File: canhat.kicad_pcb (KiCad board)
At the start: 2 copper layers, 65 x 30 mm, 37 parts, among them J1 Raspberry_Pi_2_3, J2 CAN In/Out/GND, J5 12V, U1 MCP2515-xSO, U2 SN65HVD234, U3 AT24C32-SSHM, U4 AP63205, Y1 16MHz

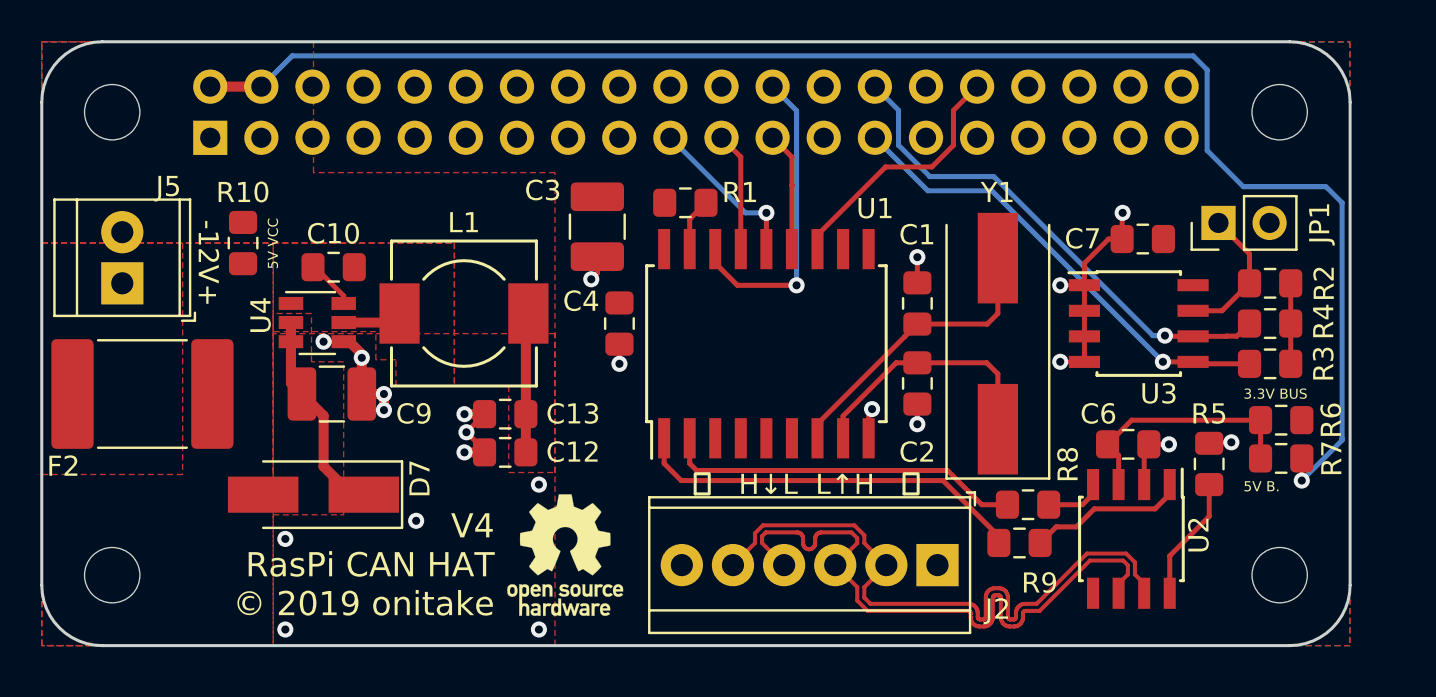
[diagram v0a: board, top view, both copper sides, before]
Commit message: Added GPIO pullups
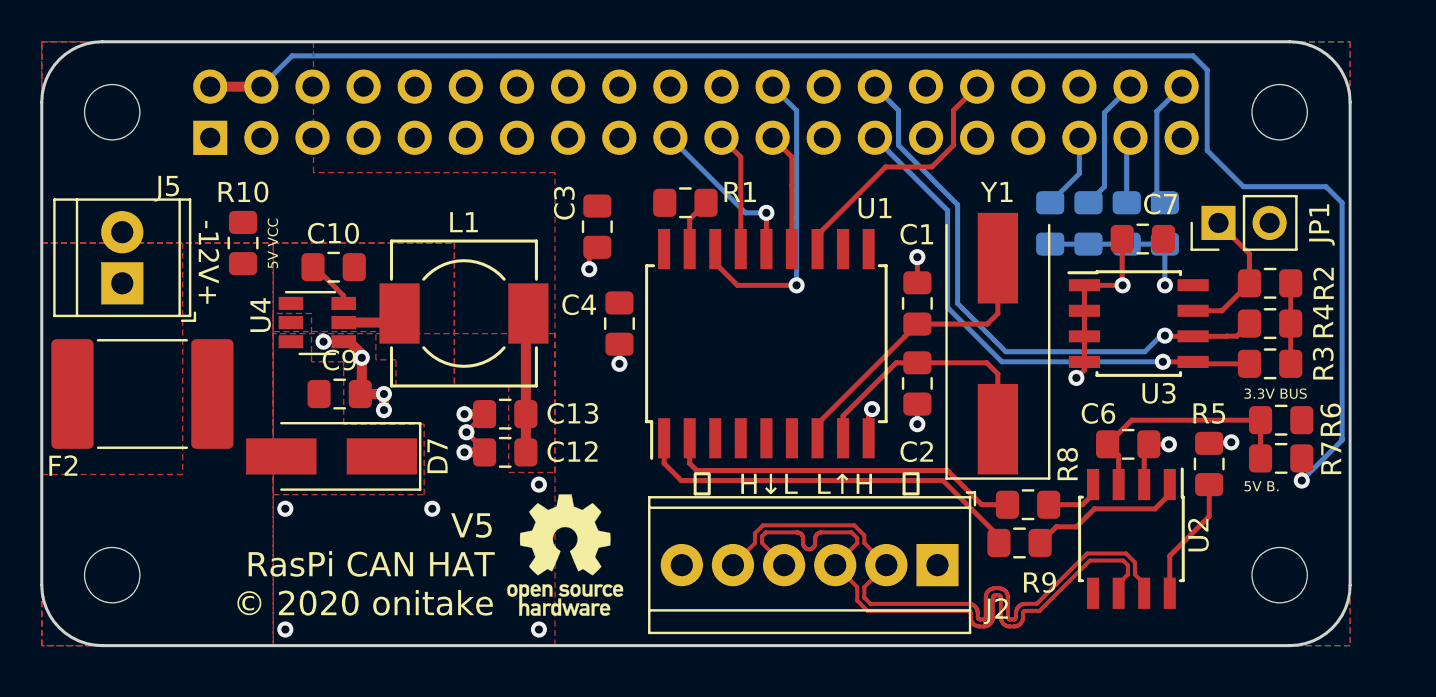
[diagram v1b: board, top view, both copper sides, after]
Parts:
- added R11: 1k, Resistor_SMD:R_0805_2012Metric_Pad1.15x1.40mm_HandSolder, B.Cu at (95.8, 59.0)
- added R12: 1k, Resistor_SMD:R_0805_2012Metric_Pad1.15x1.40mm_HandSolder, B.Cu at (92.0, 59.0)
- added R13: 1k, Resistor_SMD:R_0805_2012Metric_Pad1.15x1.40mm_HandSolder, B.Cu at (93.9, 59.0)
- added R14: 1k, Resistor_SMD:R_0805_2012Metric_Pad1.15x1.40mm_HandSolder, B.Cu at (90.1, 59.0)
- C3, C9: footprint Capacitor_SMD:C_1210_3225Metric_Pad1.42x2.65mm_HandSolder -> Capacitor_SMD:C_0805_2012Metric_Pad1.15x1.40mm_HandSolder
- moved D7 2.10 mm to (54.4, 70.6)
- moved C9 0.39 mm to (54.8, 67.5)
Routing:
- net Net-(C9-Pad1): track 13.2 -> 0.00 mm
- net +3V3: track 4.04 -> 11.8 mm, vias 0 -> 1
- net /GPIO20: track 0.00 -> 6.64 mm
- net /GPIO21: track 0.00 -> 6.45 mm
- net /GPIO19: track 0.00 -> 3.83 mm
- net /ID_SC: track 25.2 -> 28.8 mm
- net /GPIO26: track 0.00 -> 3.31 mm
- net /ID_SD: track 23.3 -> 26.1 mm
- net GND: track 31.9 -> 29.9 mm, vias 22 -> 21
- net +12V: track 0.00 -> 1.50 mm
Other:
- board text added: "V5 RasPi CAN HAT © 2020 onitake"
- board text removed: "V4 RasPi CAN HAT © 2019 onitake"

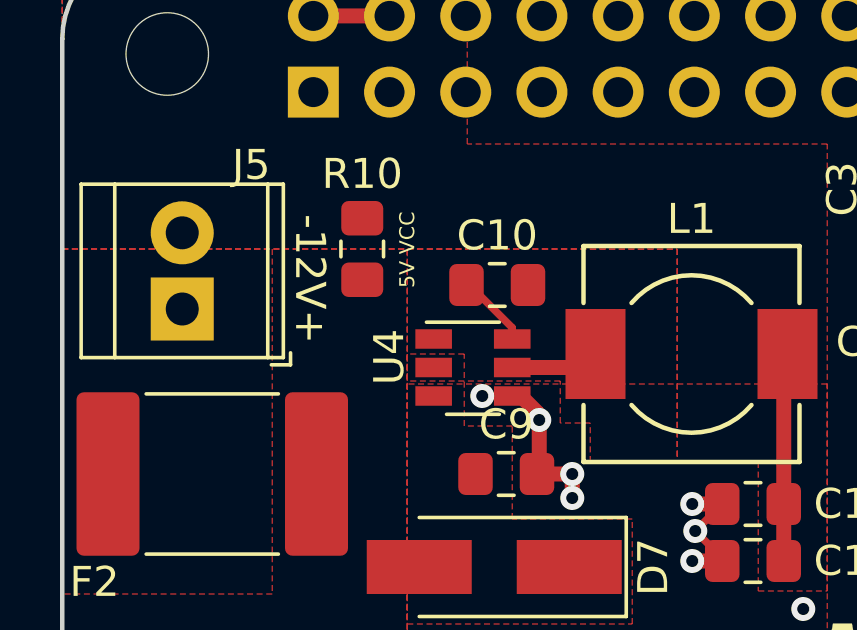
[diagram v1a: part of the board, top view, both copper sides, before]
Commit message: Fixed incorrect feedback pin wire
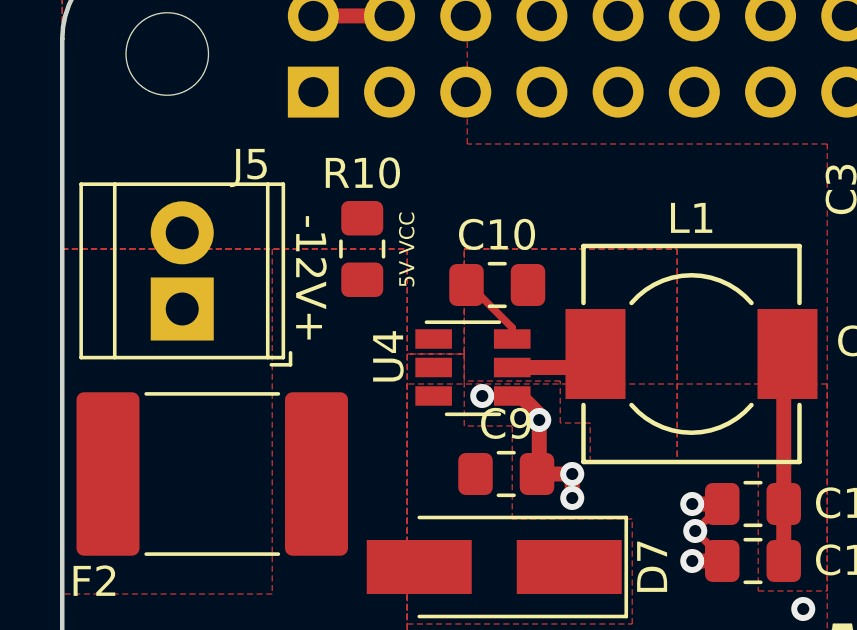
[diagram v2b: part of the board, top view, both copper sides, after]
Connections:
- R12 pad 1: /GPIO20 -> /GPIO26
- R13 pad 1: /GPIO26 -> /GPIO20
- U4 pad 1: Net-(C10-Pad2) -> +5V

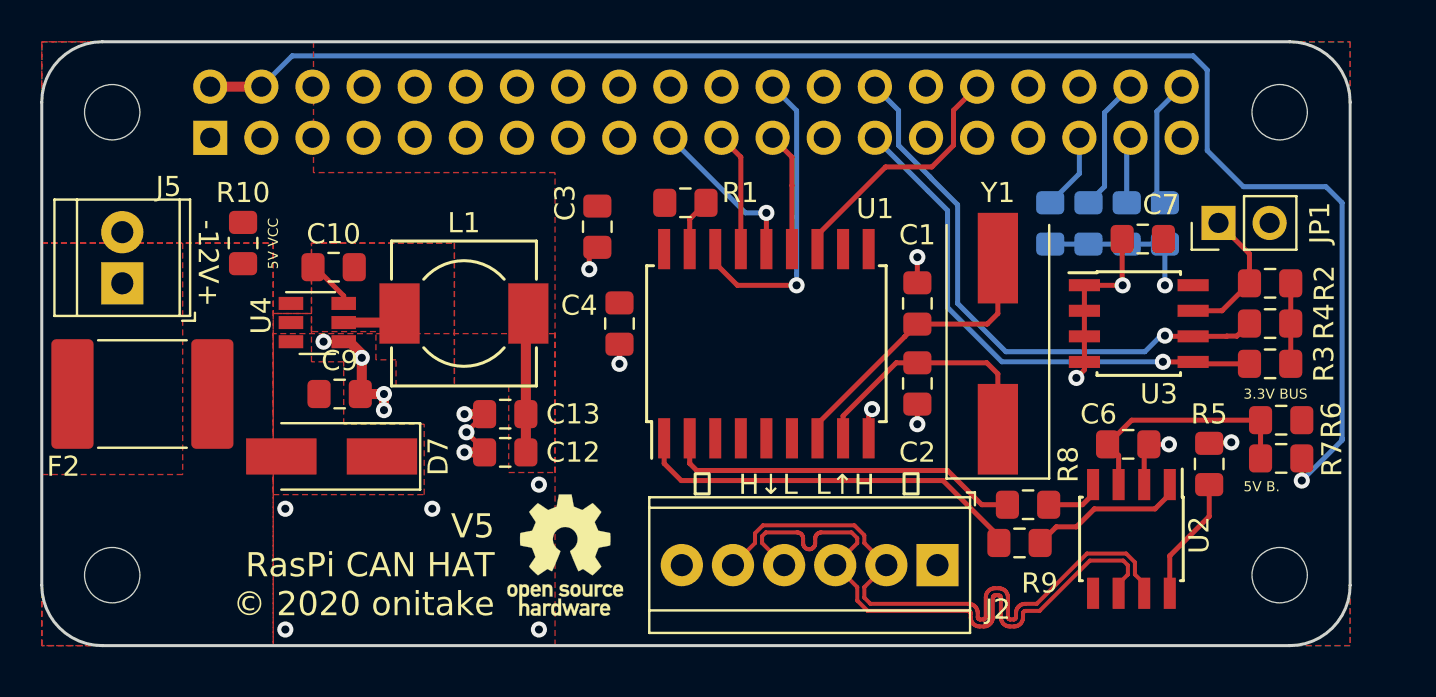
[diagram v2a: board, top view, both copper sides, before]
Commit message: Reordered parts an added GPIO pins
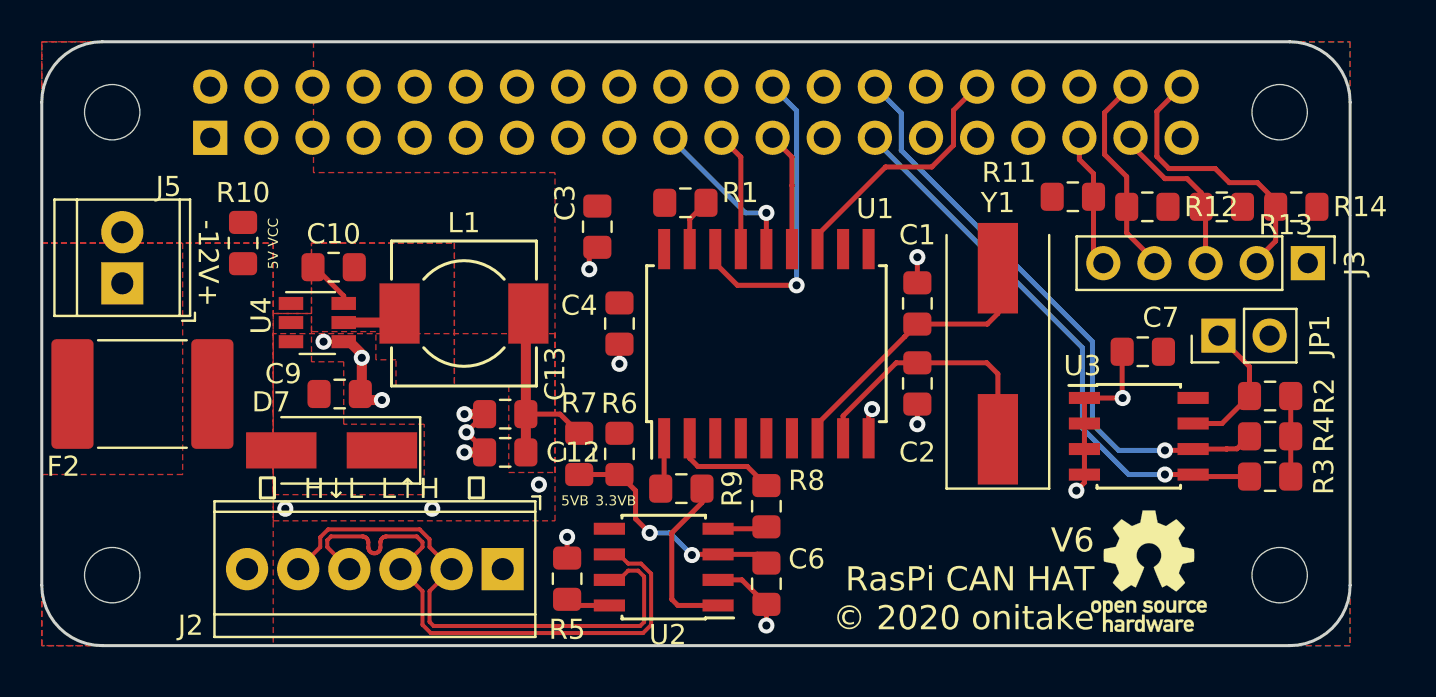
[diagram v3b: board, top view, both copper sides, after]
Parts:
- added J3: GPIO, Connector_PinHeader_2.54mm:PinHeader_1x05_P2.54mm_Vertical, F.Cu at (102.9, 61.0)
- R11, R12, R13, R14: moved to F.Cu
- moved R7 34.9 mm to (66.7, 70.5), turned to 270 degrees
- moved R6 32.9 mm to (68.7, 70.5), turned to 90 degrees
- moved R5 32.4 mm to (66.1, 76.7)
- moved OSHW1 29.0 mm to (95.0, 76.3)
- moved U2 23.3 mm to (70.9, 76.1), turned to 180 degrees
- moved J2 21.6 mm to (62.9, 76.2)
- moved C6 19.3 mm to (76.0, 76.9), turned to 270 degrees
- moved R9 17.0 mm to (71.8, 72.2)
- moved R8 13.0 mm to (76.0, 73.1), turned to 270 degrees
- moved R14 12.3 mm to (102.3, 58.2), turned to 0 degrees
- moved C7 5.60 mm to (94.7, 65.4)
- moved JP1 5.60 mm to (98.5, 64.6)
- moved R2 5.60 mm to (101.0, 67.6)
- moved R3 5.60 mm to (101.0, 71.6)
- moved R4 5.60 mm to (101.0, 69.6)
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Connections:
- D7 pad 2: +12V -> +12LF
- F2 pad 1: Net-(F2-Pad1) -> +12V
- F2 pad 2: +12V -> +12LF
- J5 pad 1: Net-(F2-Pad1) -> +12V
- R10 pad 2: +12V -> +12LF
- R11 pad 1: /GPIO21 -> /GPIO19
- R12 pad 1: /GPIO26 -> /GPIO20
- R13 pad 1: /GPIO20 -> /GPIO26
- R14 pad 1: /GPIO19 -> /GPIO21
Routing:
- net +5V: track 84.8 -> 9.89 mm, vias 1 -> 0
- net Net-(R9-Pad1): track 20.0 -> 2.57 mm
- net Net-(R8-Pad1): track 17.9 -> 5.36 mm
- net /GPIO21: track 6.45 -> 14.3 mm
- net +3V3: track 11.8 -> 4.04 mm, vias 1 -> 0
- net /GPIO26: track 3.31 -> 8.69 mm
- net /CAN_P: track 32.0 -> 28.0 mm
- net Net-(R5-Pad2): track 6.21 -> 2.23 mm
- net /GPIO20: track 6.64 -> 10.3 mm
- net /GPIO19: track 3.83 -> 6.72 mm
- net /CAN_N: track 32.0 -> 29.7 mm
- net /ID_SD: track 26.1 -> 28.0 mm
- net +12V: track 1.50 -> 0.00 mm
- net +12LF: track 0.00 -> 1.50 mm
- net /ID_SC: track 28.8 -> 30.1 mm
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- added copper zone on F.Cu, net +12LF
- removed copper zone on F.Cu, net Net-(F2-Pad1)
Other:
- board text added: "3.3VB"
- board text added: "5VB"
- board text added: "V6 RasPi CAN HAT © 2020 onitake"
- board text removed: "3.3V BUS"
- board text removed: "5V B."
- board text removed: "V5 RasPi CAN HAT © 2020 onitake"

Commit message: Move parts a bit
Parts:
- moved R11 0.92 mm to (90.3, 57.7)
- moved C12 0.80 mm to (63.0, 69.6)
- moved C10 0.80 mm to (54.5, 60.4)
- moved U4 0.80 mm to (53.7, 63.1)
- moved C13 0.80 mm to (63.0, 67.7)
- moved C9 0.80 mm to (54.8, 66.7)
- moved D7 0.80 mm to (54.4, 69.5)
- moved L1 0.80 mm to (61.0, 62.7)
- moved R14 0.73 mm to (101.6, 58.2)
- moved R12 0.72 mm to (94.2, 58.2)
- moved R13 0.72 mm to (97.9, 58.2)
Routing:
- net GND: track 30.0 -> 20.2 mm, vias 18 -> 14
- net +12LF: track 1.50 -> 5.01 mm
- net /GPIO21: track 14.3 -> 13.3 mm
- net /CAN_N: track 29.7 -> 28.8 mm
- net /CAN_P: track 28.0 -> 28.8 mm
- net /GPIO26: track 8.69 -> 8.04 mm
- net /TX: track 8.55 -> 8.05 mm, vias 0 -> 2
- net VBUS: track 12.0 -> 12.1 mm, vias 2 -> 0
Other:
- board text added: "CAN HAT V6 Raspberry Pi ©2020 onitake"
- board text removed: "V6 RasPi CAN HAT © 2020 onitake"

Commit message: More finetuning
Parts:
- moved OSHW1 13.9 mm to (81.1, 76.0)
- moved R5 1.47 mm to (66.1, 75.2)
- moved Y1 0.70 mm to (87.5, 66.2)
- moved R11 0.54 mm to (90.1, 58.2)
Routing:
- net GND: track 20.2 -> 17.9 mm, vias 14 -> 18
- net Net-(C1-Pad1): track 14.7 -> 12.6 mm
- net /ID_SD: track 28.0 -> 29.1 mm
- net Net-(R5-Pad2): track 2.23 -> 3.23 mm
- net +5V: track 9.50 -> 8.55 mm
- net /TX: track 8.05 -> 7.22 mm, vias 2 -> 0
- net VBUS: track 12.1 -> 12.8 mm, vias 0 -> 2
- net Net-(C2-Pad2): track 12.9 -> 13.6 mm
- net /ID_SC: track 30.1 -> 30.6 mm

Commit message: Some more finetunings
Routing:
- net GND: vias 18 -> 17

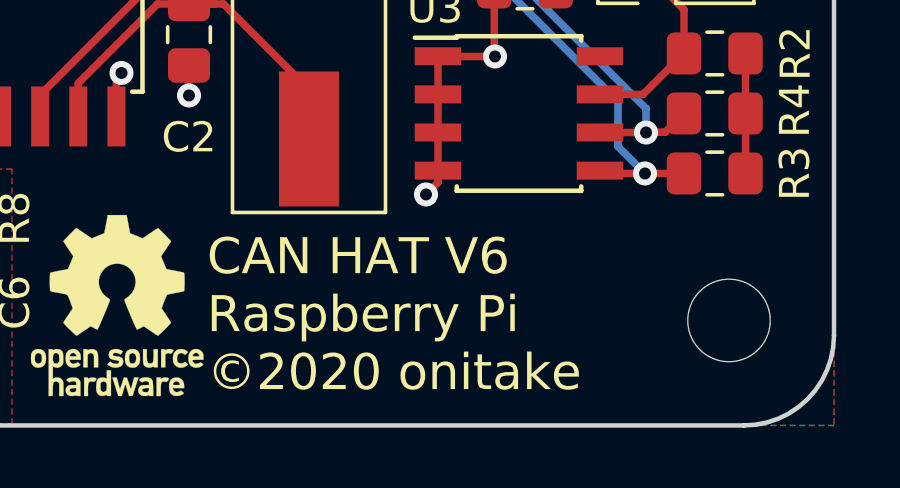
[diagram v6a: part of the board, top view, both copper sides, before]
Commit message: Corrected Raspberry Pi branding
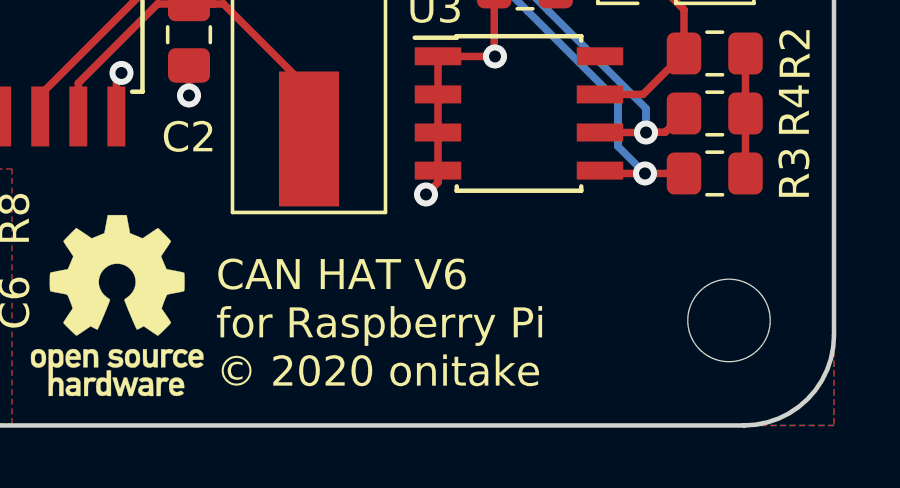
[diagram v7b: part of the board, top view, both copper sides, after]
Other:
- board text added: "CAN HAT V6 for Raspberry Pi © 2020 onitake"
- board text removed: "CAN HAT V6 Raspberry Pi ©2020 onitake"

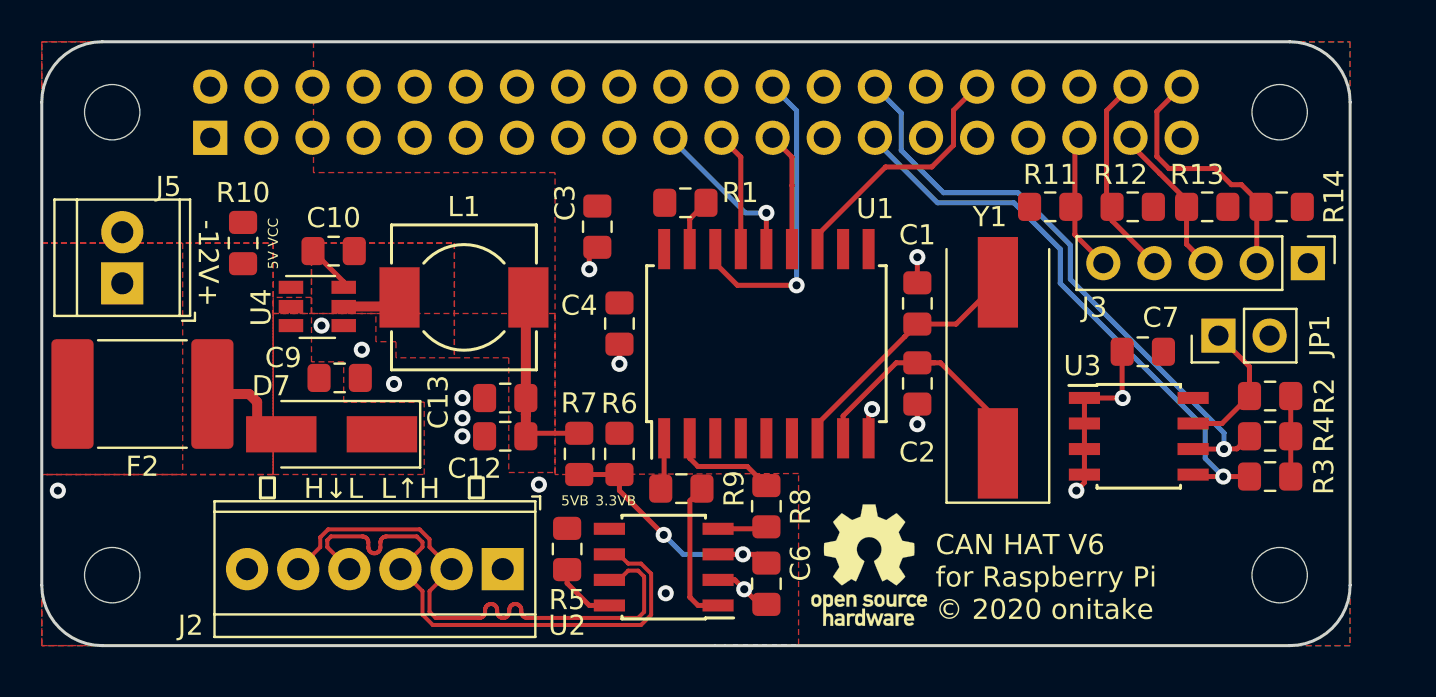
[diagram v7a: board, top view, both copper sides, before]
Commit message: Use 5V transceiver with 3V logic and some finetuning
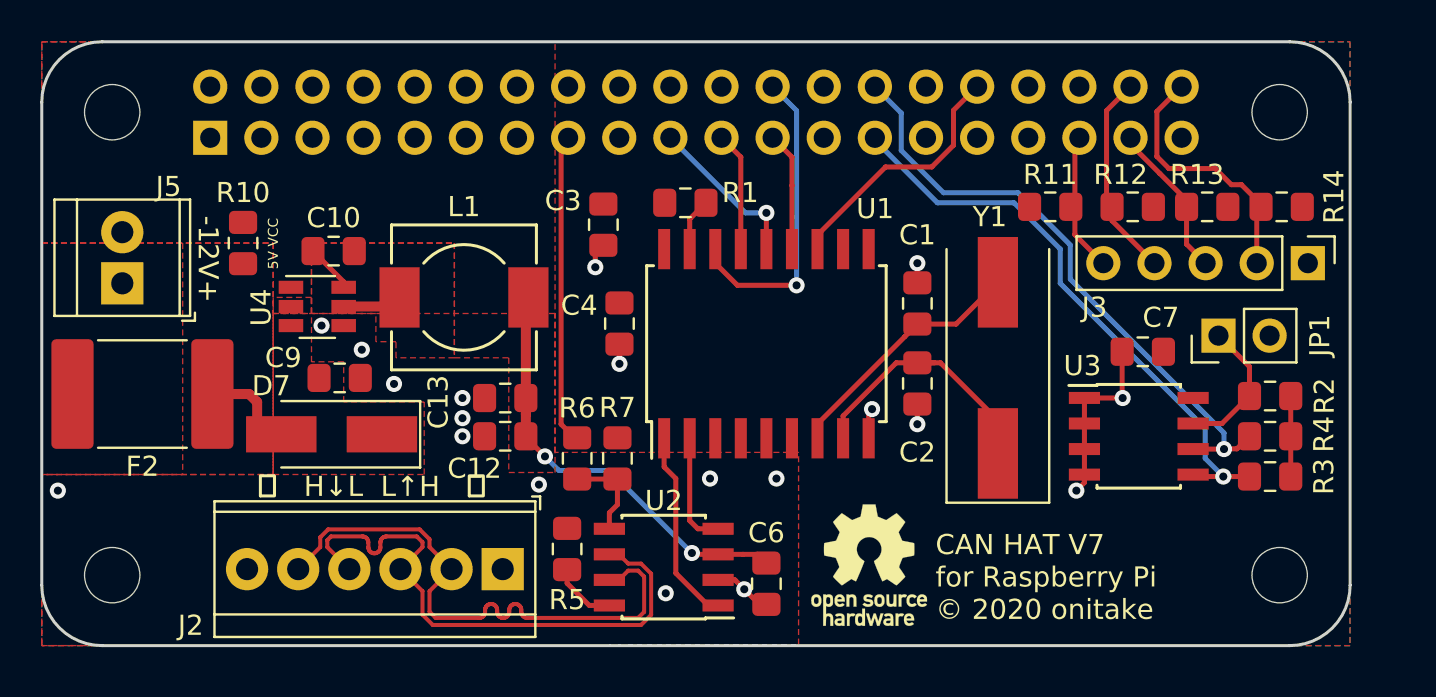
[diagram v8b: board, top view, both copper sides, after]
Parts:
- removed R8, R9: 1k, Resistor_SMD:R_0805_2012Metric_Pad1.15x1.40mm_HandSolder
- R6: value DNP/0 -> DNP
- R7: value 0/DNP -> 0
- U2: value SN65HVD234 -> SN65HVDA541
- moved R6 2.11 mm to (66.6, 70.7)
- moved R7 1.91 mm to (68.6, 70.7)
- moved C3 0.32 mm to (67.9, 59.1)
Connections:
- C6 pad 1: VBUS -> +5V
- J1 pad 15: (no net) -> /TRXEN
- R6 pad 1: VBUS -> Net-(R6-Pad1)
- R6 pad 2: +3V3 -> /TRXEN
- R7 pad 1: +5V -> +3V3
- R7 pad 2: VBUS -> Net-(R6-Pad1)
- U1 pad 1: Net-(R9-Pad1) -> /TX
- U1 pad 2: Net-(R8-Pad1) -> /RX
- U2 pad 3: VBUS -> +5V
- U2 pad 5: (no net) -> Net-(R6-Pad1)
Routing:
- net /TRXEN: track 0.00 -> 15.5 mm
- net VBUS: track 12.8 -> 0.00 mm, vias 2 -> 0
- net +5V: track 8.55 -> 20.5 mm, vias 0 -> 2
- net Net-(R8-Pad1): track 5.36 -> 0.00 mm
- net Net-(R6-Pad1): track 0.00 -> 4.64 mm
- net /RX: track 2.44 -> 5.67 mm
- net Net-(R9-Pad1): track 2.57 -> 0.00 mm
- net /TX: track 7.22 -> 9.71 mm
- net GND: track 17.9 -> 17.6 mm, vias 17 -> 19
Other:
- board text added: "CAN HAT V7 for Raspberry Pi © 2020 onitake"
- board text removed: "3.3VB"
- board text removed: "5VB"
- board text removed: "CAN HAT V6 for Raspberry Pi © 2020 onitake"
